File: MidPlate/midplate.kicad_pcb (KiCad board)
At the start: 2 copper layers, 180 x 150 mm, 77 parts, among them J1 XT60, J12 JST_B4B-XH-A, J13 JST_BM04B-GHS-TBT, J2 XT60, J4 TE_2-1445053-2_2PIN, J5 TE_2-1445053-2_2PIN, J7 1586842-6, J9 JST_BM04B-GHS-TBT, Q1 MCU60P04-TP, Q2 MCU60P04-TP, SW1 RA1H1C112R, U1 LMR23630AFDDAR

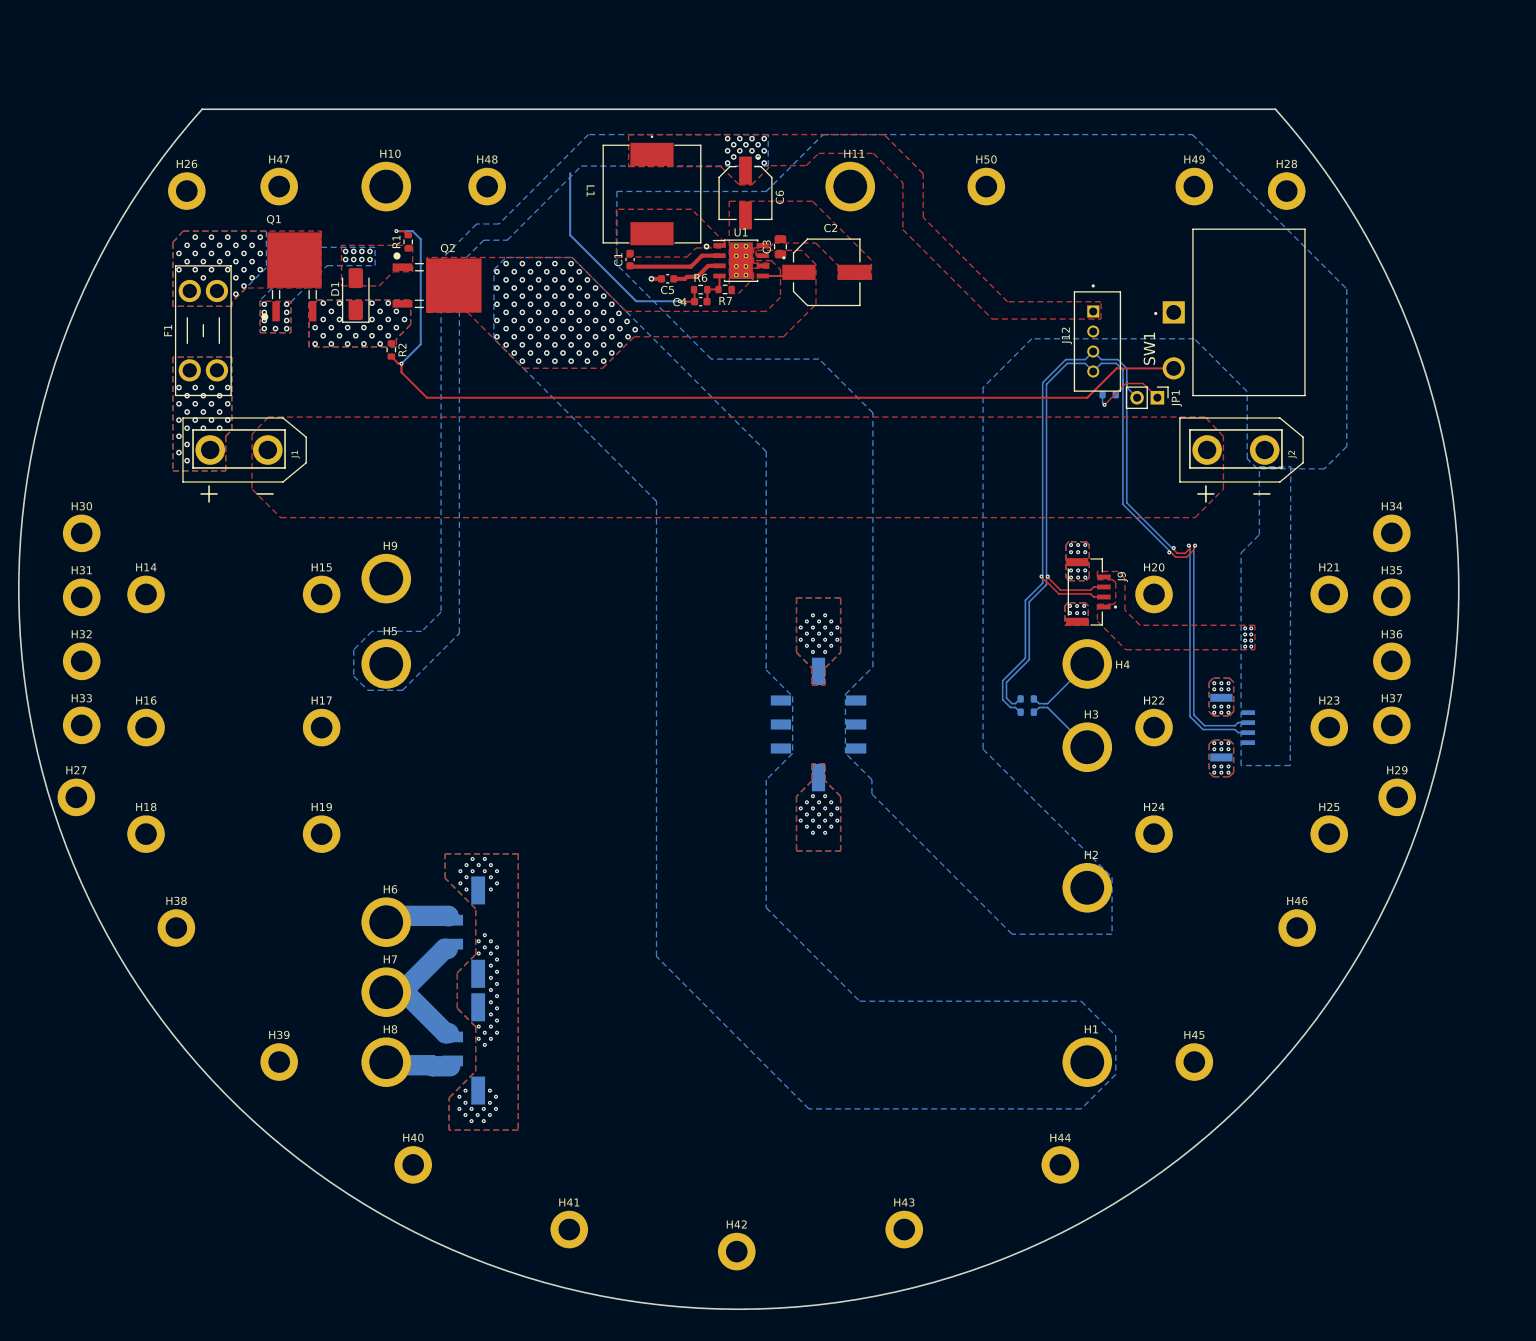
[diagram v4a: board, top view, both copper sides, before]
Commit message: update to midplate hole placements
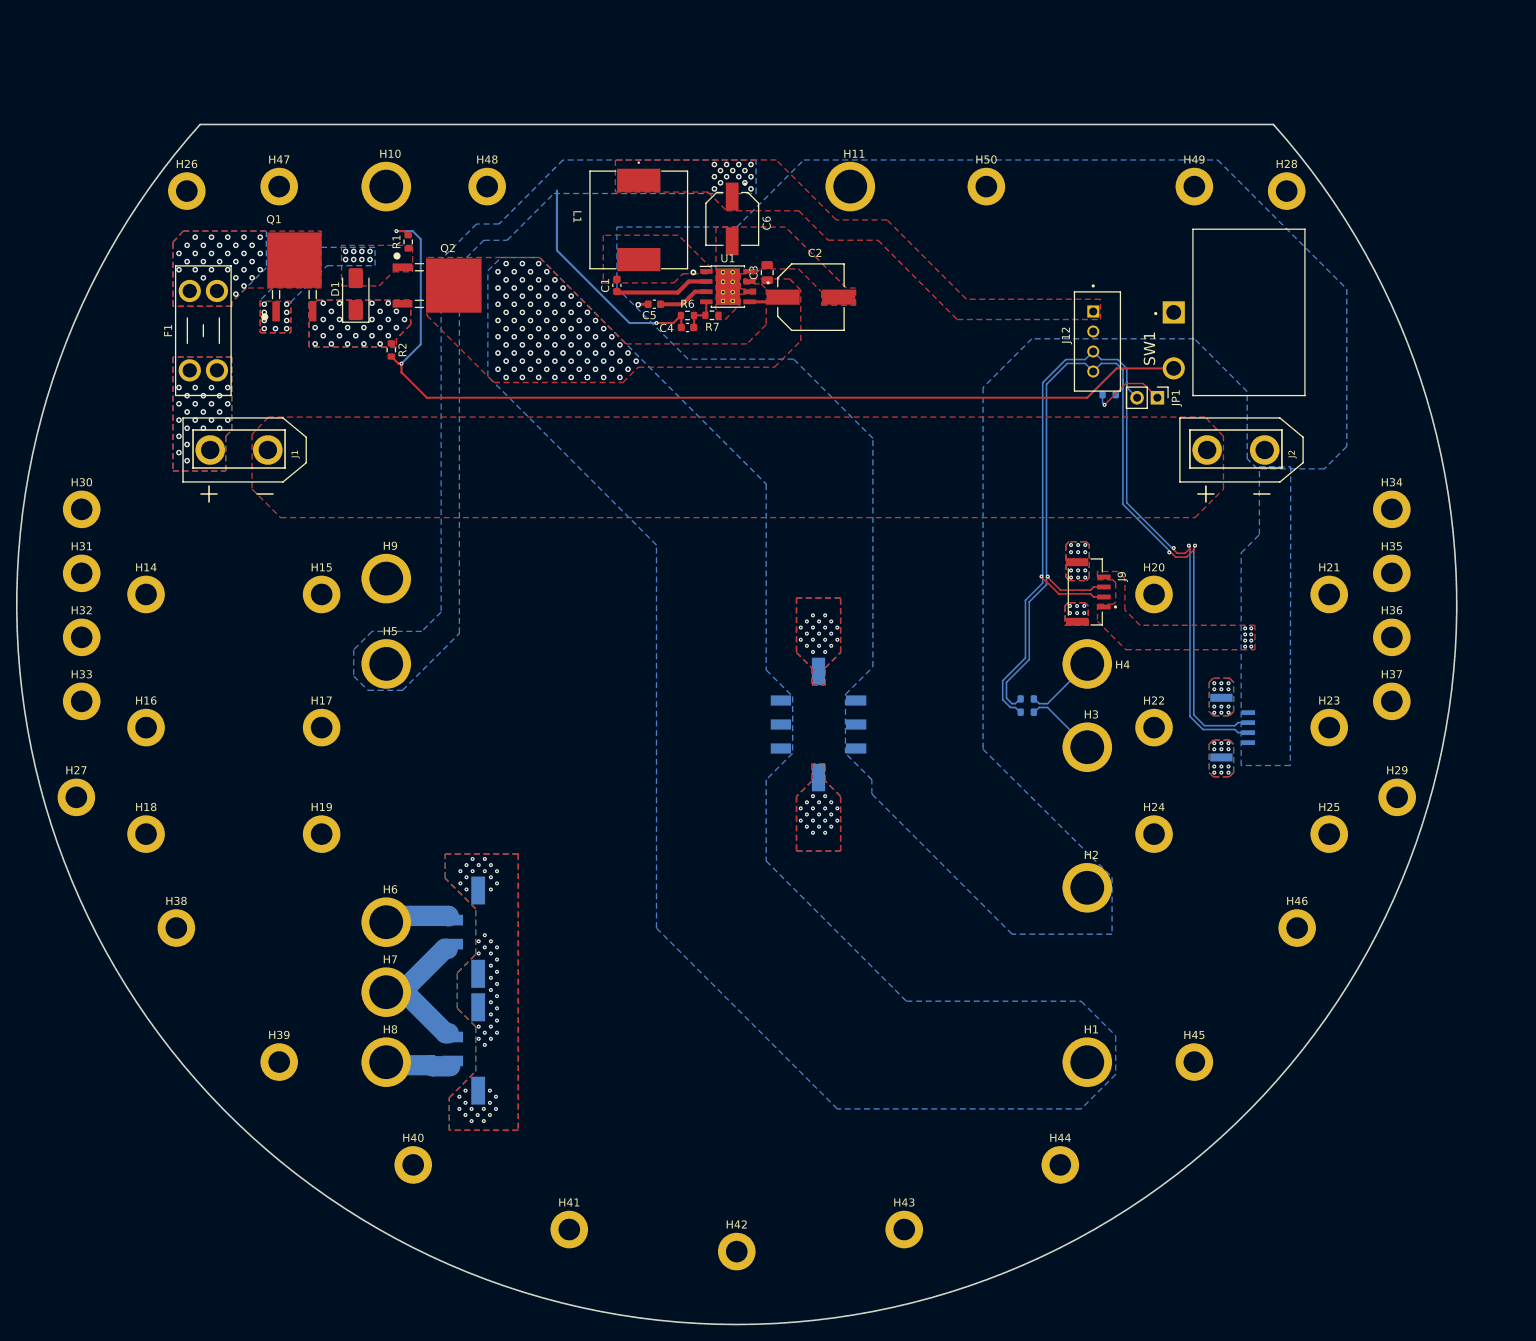
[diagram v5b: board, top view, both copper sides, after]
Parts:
- moved C2 3.68 mm to (146.9, 43.8)
- moved R6 3.63 mm to (131.5, 46.1)
- moved U1 3.63 mm to (136.6, 42.5)
- moved C1 3.63 mm to (122.7, 42.3)
- moved C4 3.63 mm to (131.5, 47.6)
- moved R7 3.63 mm to (134.6, 46.1)
- moved C3 3.63 mm to (141.5, 40.7)
- moved C6 3.63 mm to (137.1, 34.0)
- moved L1 3.63 mm to (125.4, 34.2)
- moved C5 3.58 mm to (127.4, 44.7)
- moved H30 3.00 mm to (55.8, 70.3)
- moved H31 3.00 mm to (55.8, 78.3)
- moved H32 3.00 mm to (55.8, 86.3)
- moved H33 3.00 mm to (55.8, 94.3)
- moved H34 3.00 mm to (219.6, 70.3)
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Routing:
- net VCC: track 4.72 -> 4.45 mm, vias 95 -> 99

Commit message: power board and midplate updates (mostly finalized)
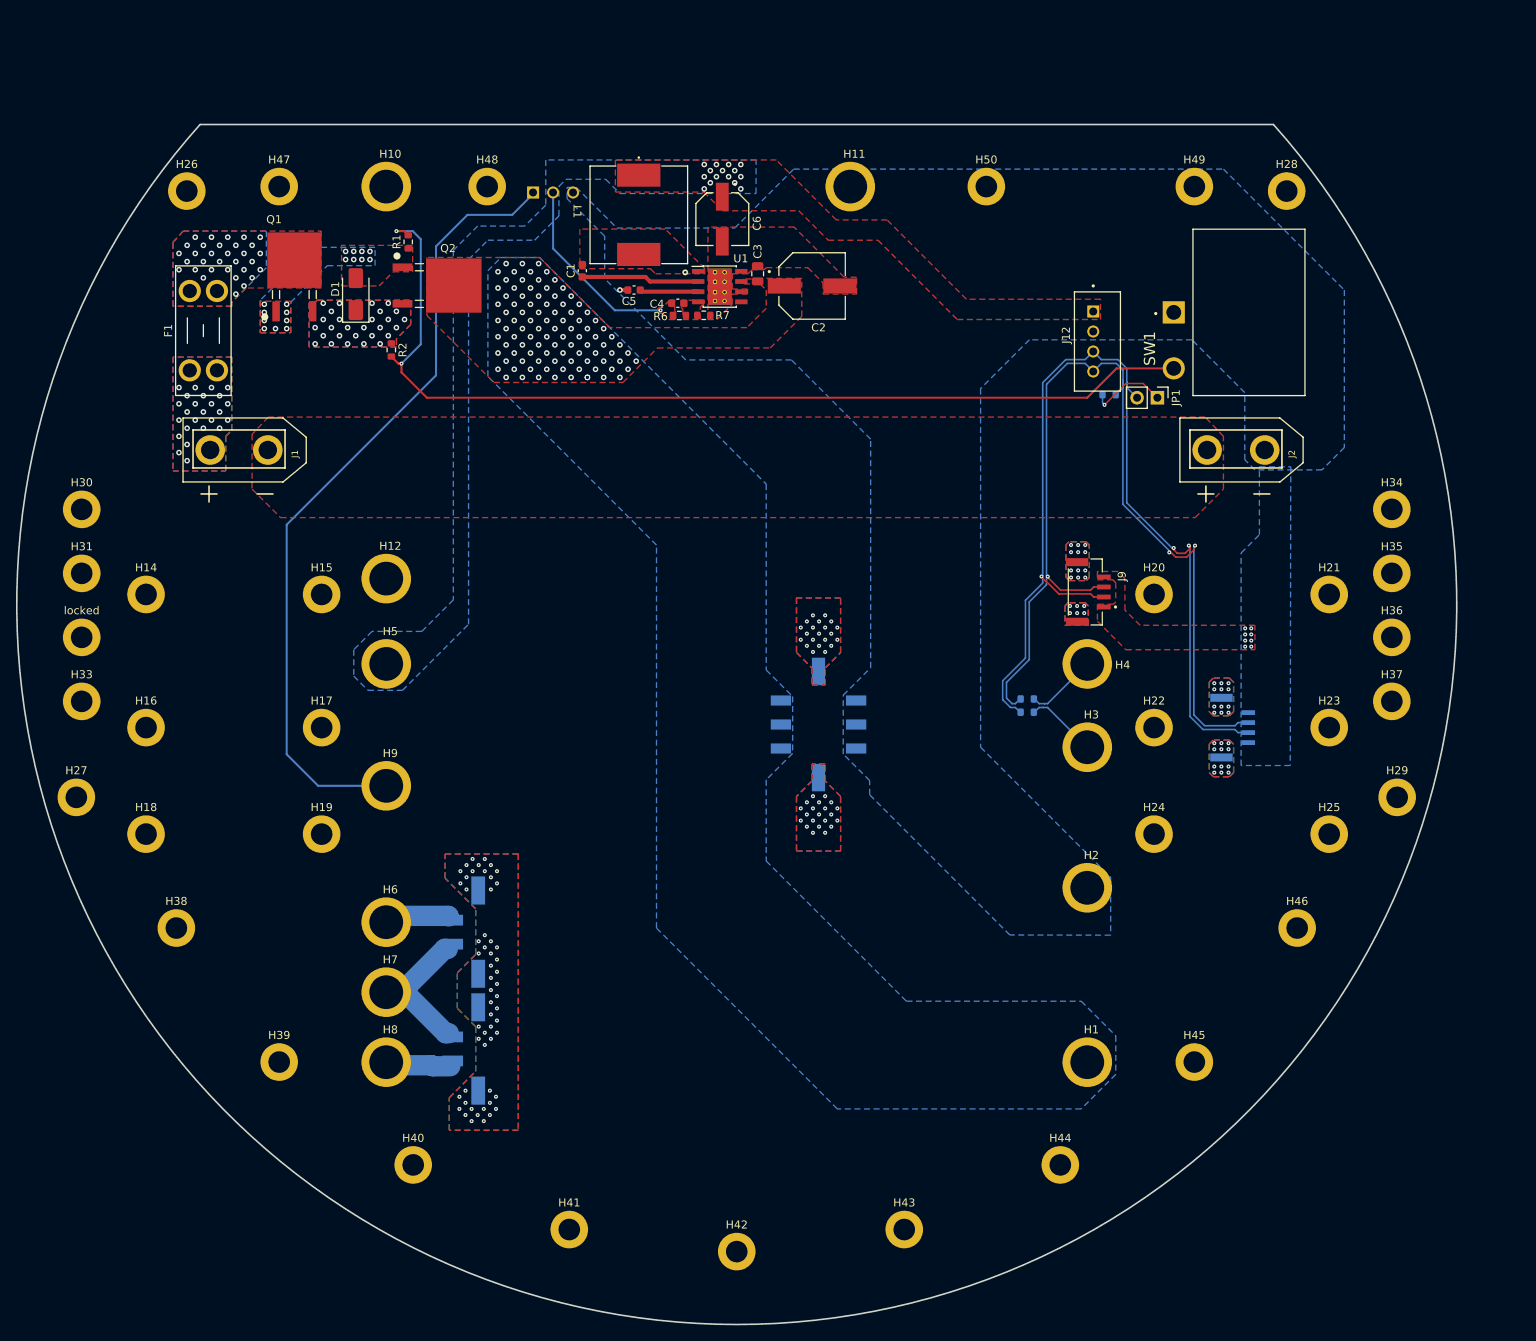
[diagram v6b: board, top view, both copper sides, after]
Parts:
- added H9: SMTSO2515CTJ, bots:SMTSO2515CTJ, F.Cu at (93.9, 104.9)
- added J3: JST_B3B-XH-A, bots:JST_B3B-XH-A, B.Cu at (114.7, 31.3)
- moved C1 4.69 mm to (118.4, 40.5)
- moved C4 3.27 mm to (130.3, 44.6)
- moved C5 3.10 mm to (124.8, 42.9)
- moved C2 1.40 mm to (147.1, 42.4)
- moved C6 1.24 mm to (135.9, 34.1)
- moved C3 1.20 mm to (140.3, 40.9)
- moved R6 1.02 mm to (130.5, 46.1)
- moved R7 1.02 mm to (133.5, 46.1)
- moved U1 1.02 mm to (135.5, 42.5)
- moved L1 0.64 mm to (125.4, 33.5)
- renumbered H9 to H12, H32 to locked
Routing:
- net BKBM: track 0.00 -> 100.3 mm
- net +5V: track 28.7 -> 23.7 mm
- net /Power Input/FB: track 4.68 -> 0.00 mm
- net VCC: track 4.45 -> 0.00 mm
- net /Power Input/BOOT: track 11.8 -> 14.7 mm
- net /Power Input/U1_VCC: track 6.37 -> 7.45 mm
- added copper zone on F.Cu, net /Power Input/FB

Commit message: midplate
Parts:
- H1: value SMTSO2515CTJ -> VCC
- H10, H11, H12: value SMTSO2515CTJ -> RPI
- H2: value SMTSO2515CTJ -> GND
- H3: value SMTSO2515CTJ -> CANL
- H4: value SMTSO2515CTJ -> CANH
- H5: value SMTSO2515CTJ -> 5V
- H6: value SMTSO2515CTJ -> EXTRA
- H7: value SMTSO2515CTJ -> HV
- H8: value SMTSO2515CTJ -> CHICKER
- H9: value SMTSO2515CTJ -> BKBM

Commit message: updates
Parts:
- moved C4 0.71 mm to (130.3, 43.9)
- moved R6 0.71 mm to (130.5, 45.4)
- moved U1 0.71 mm to (135.5, 41.8)
- moved R7 0.71 mm to (133.5, 45.4)
- moved C2 0.66 mm to (147.1, 41.8)
- moved C3 0.64 mm to (140.3, 40.3)
- moved C5 0.36 mm to (125.0, 42.6)
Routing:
- net VCC: track 0.00 -> 4.35 mm
